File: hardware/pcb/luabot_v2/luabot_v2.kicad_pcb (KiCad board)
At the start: 2 copper layers, 67.8 x 32.1 mm, 26 parts, among them CON1 BAT_IN, P2 GND_GPIO, P3 VCC_GPIO, SW1 RESET, U1 ESP-07V2, U2 LM1117

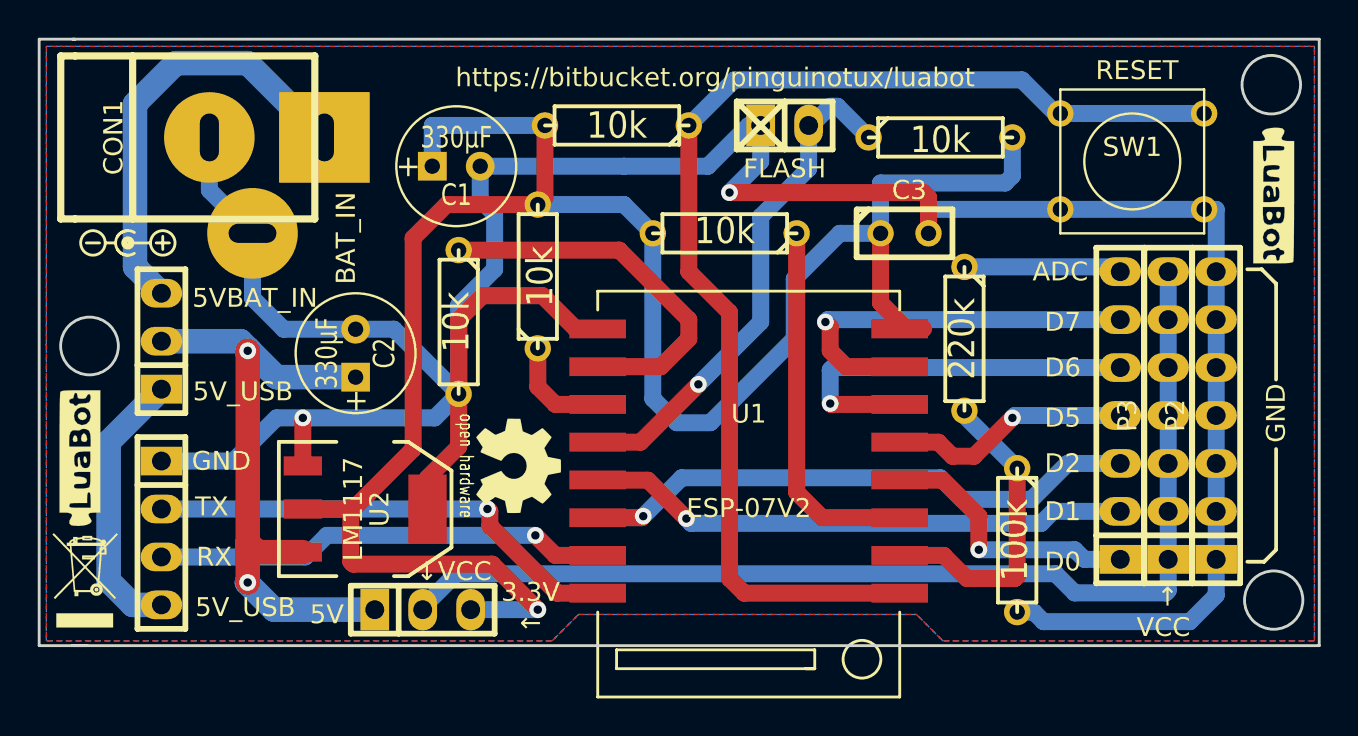
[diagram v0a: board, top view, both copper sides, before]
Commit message: Actualización PCB luabot_v2
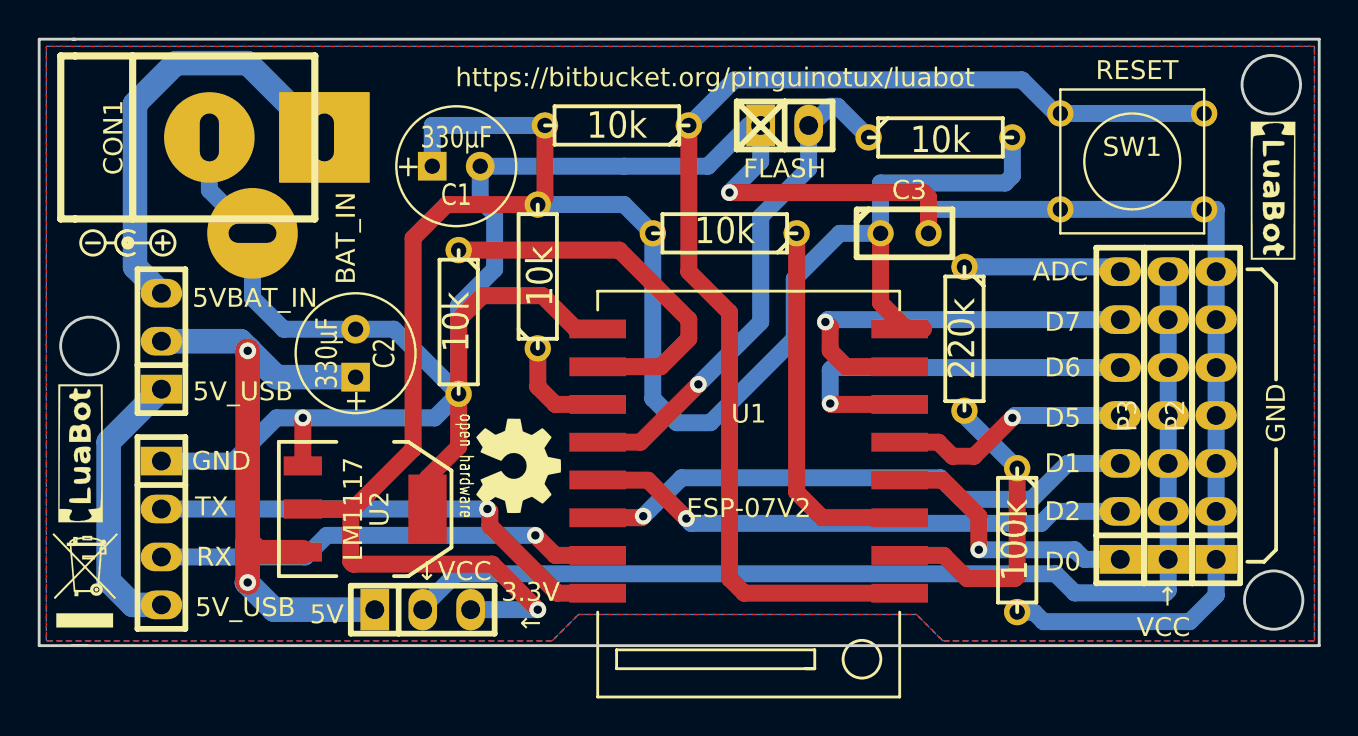
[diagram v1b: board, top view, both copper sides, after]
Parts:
- removed the G*** at (21.1, 41.1)
- removed the G*** at (84.3, 27.2)
- added G***: LOGO, cp_luabot_v2:logo_v2, F.Cu at (21.1, 40.9)
- added G***: LOGO, cp_luabot_v2:logo_v2, F.Cu at (84.3, 26.9)
